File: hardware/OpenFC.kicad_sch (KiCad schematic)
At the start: 0 parts

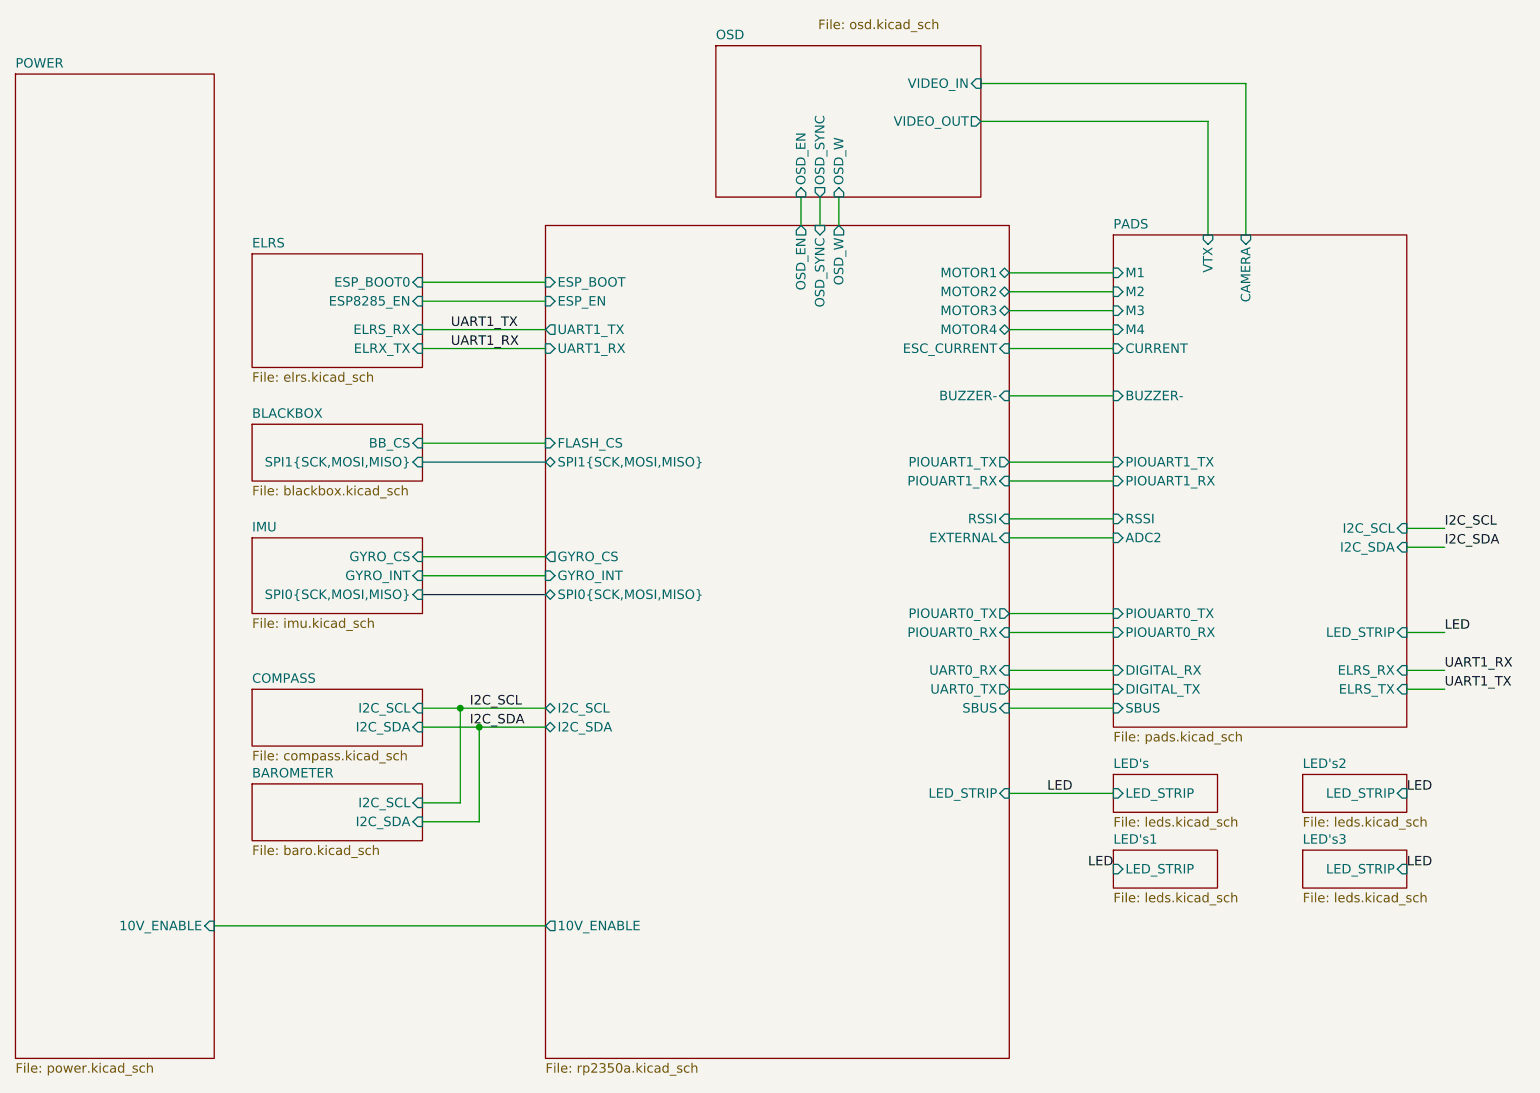
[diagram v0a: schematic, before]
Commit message: Standardize repo: .gitignore, README, license, remove orphaned files
- Standardize .gitignore to match ecosystem template
- Fix README: correct GitHub URL, remove generic sections, remove nonexistent dirs
- Replace LICENSE stub with full CERN-OHL-S-2.0 text
- Remove orphaned schematics (baro, blackbox, compass, elrs, leds) — not in ECO variant
- Delete self-referential symlink and parent OpenFC production leftovers
- Add new footprints and 3D models (SIM, TF connectors)

Co-Authored-By: Claude Opus 4.6 (1M context) <noreply@anthropic.com>
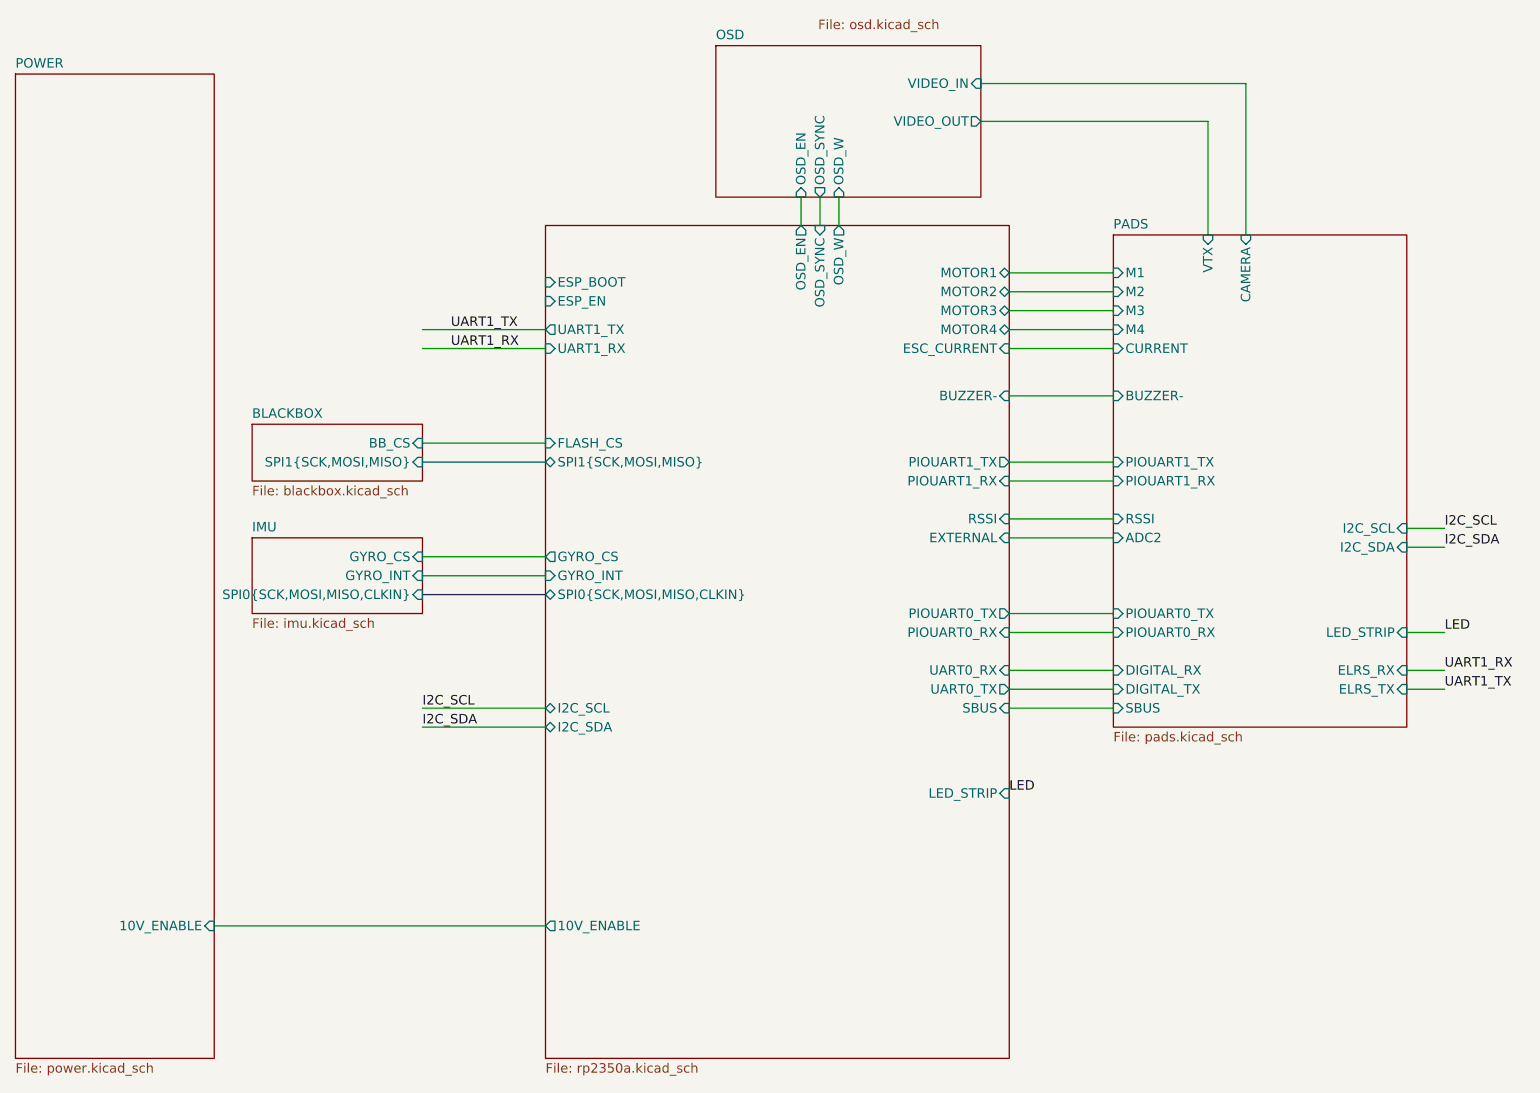
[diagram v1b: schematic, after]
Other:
- removed sheet BAROMETER
- removed sheet COMPASS
- removed sheet ELRS
- removed sheet LED's
- removed sheet LED's1
- removed sheet LED's2
- removed sheet LED's3
- sheet IMU ports: added SPI0{SCK,MOSI,MISO,CLKIN}; removed SPI0{SCK,MOSI,MISO}
- sheet RP2350A ports: added SPI0{SCK,MOSI,MISO,CLKIN}; removed SPI0{SCK,MOSI,MISO}

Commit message: Add V0.3 known issues for V0.4 fix list, update open issues
C28 voltage rating, R30 divider, L2 inductor value, LED0 color,
LMR51430 upgrade path — all noted for next revision. CRIT-5 (ESC
connector) marked fixed. OSD pin mapping updated to GPIO4-6.

Co-Authored-By: Claude Opus 4.6 (1M context) <noreply@anthropic.com>
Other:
- sheet BLACKBOX ports: added FLASH_CS; removed BB_CS
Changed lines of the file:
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@@
 			)
 		)
-		(pin "BB_CS" input
-			(at 86.36 80.01 0)
+		(pin "SPI1{SCK,MOSI,MISO}" input
+			(at 86.36 82.55 0)
 			(effects
 				(font
@@
 			)
 		)
-		(pin "SPI1{SCK,MOSI,MISO}" input
-			(at 86.36 82.55 0)
+		(pin "FLASH_CS" input
+			(at 86.36 80.01 0)
 			(effects
 				(font
